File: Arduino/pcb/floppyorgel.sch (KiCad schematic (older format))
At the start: 2 parts, among them J1 VCC_Power_Select

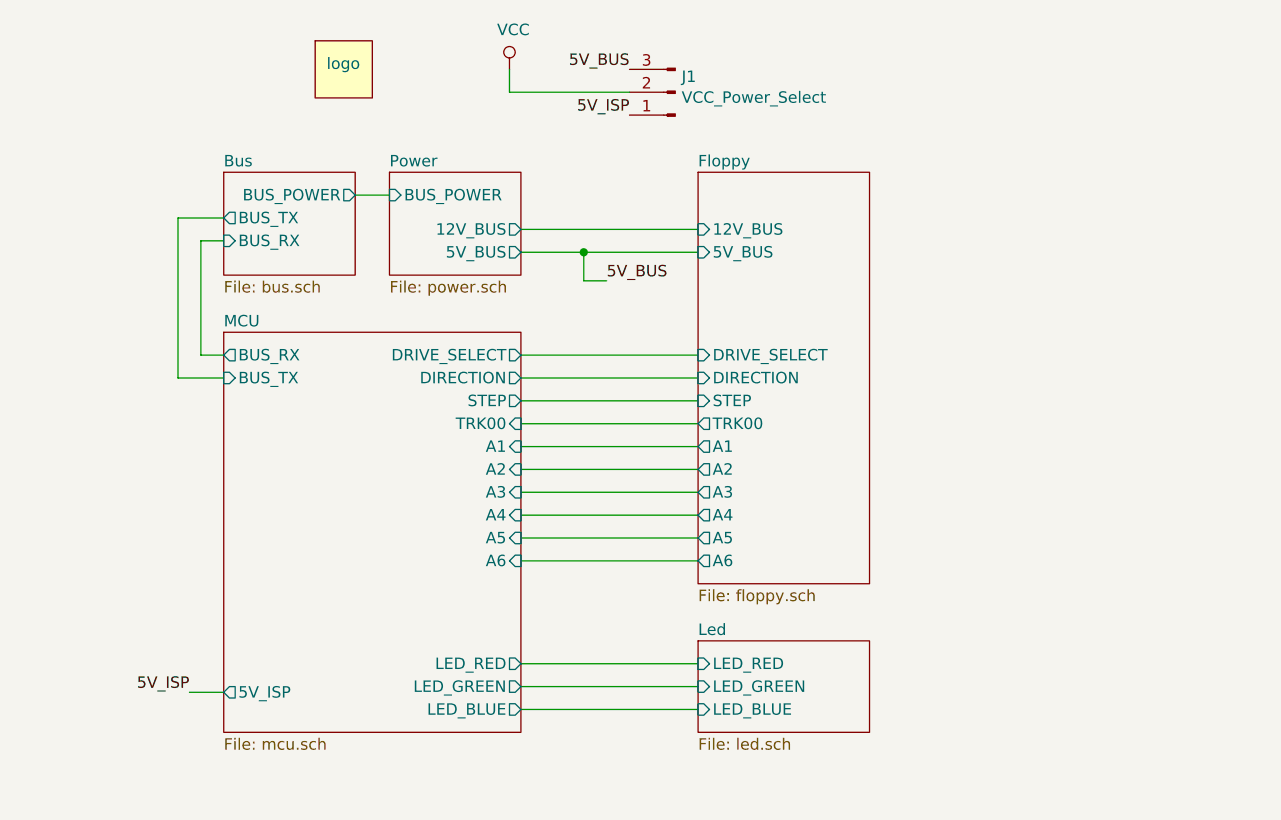
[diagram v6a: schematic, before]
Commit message: pcb: route RS485 control pins
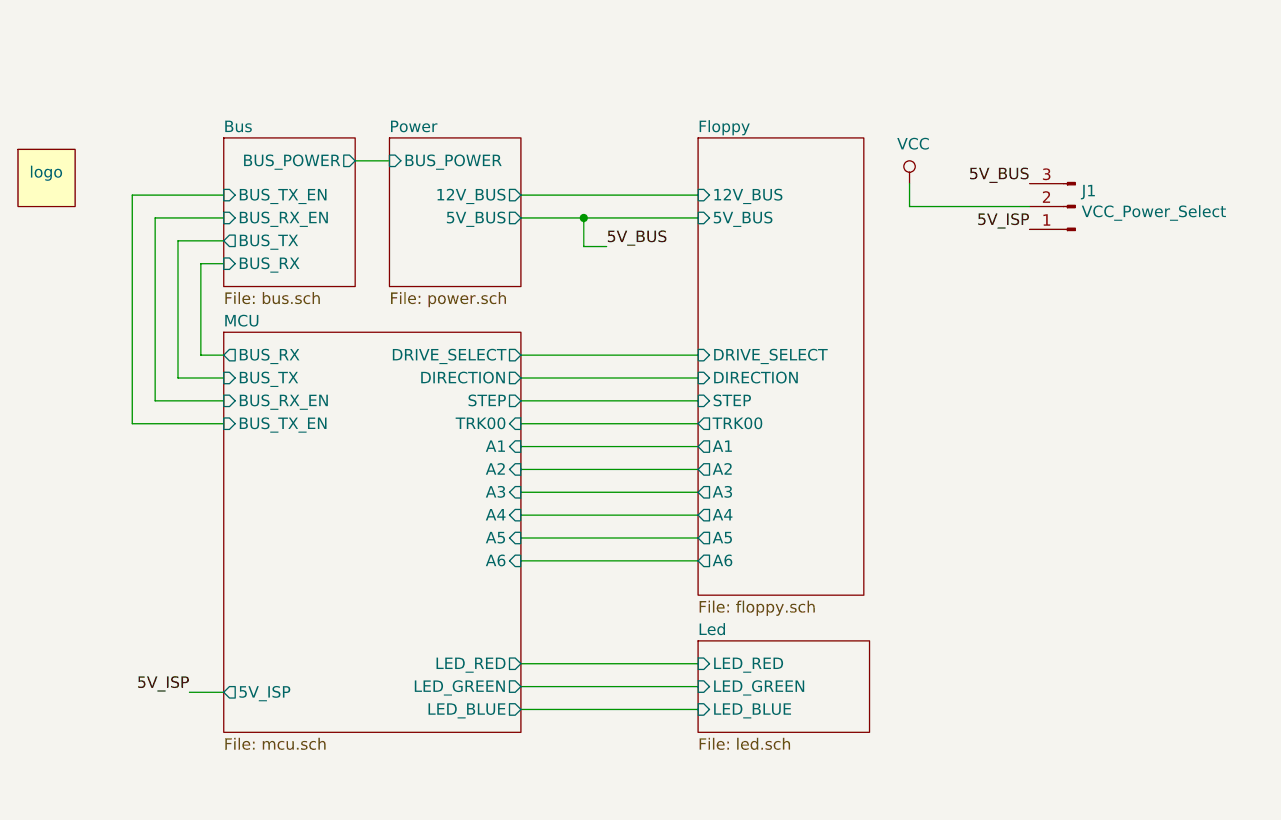
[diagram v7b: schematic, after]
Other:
- moved on the sheet: J1
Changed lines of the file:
@@
 $EndDescr
 $Sheet
-S 3725 2775 575  450
-U 5CD1E0A5
-F0 "Bus" 50
-F1 "bus.sch" 50
-F2 "BUS_POWER" O R 4300 2875 50
-F3 "BUS_TX" O L 3725 2975 50
-F4 "BUS_RX" I L 3725 3075 50
-$EndSheet
-$Sheet
-S 4450 2775 575  450
+S 4450 2625 575  650
 U 5CD31258
 F0 "Power" 50
 F1 "power.sch" 50
-F2 "BUS_POWER" I L 4450 2875 50
-F3 "12V_BUS" O R 5025 3025 50
-F4 "5V_BUS" O R 5025 3125 50
+F2 "BUS_POWER" I L 4450 2725 50
+F3 "12V_BUS" O R 5025 2875 50
+F4 "5V_BUS" O R 5025 2975 50
 $EndSheet
 Wire Wire Line
@@
 	3725 3675 3525 3675
 Wire Wire Line
-	4300 2875 4450 2875
-Wire Wire Line
-	3725 3075 3625 3075
-Wire Wire Line
-	3625 3075 3625 3575
-Wire Wire Line
-	3525 2975 3725 2975
-Wire Wire Line
-	3525 2975 3525 3675
-Wire Wire Line
-	5025 3025 5800 3025
-Wire Wire Line
 	5025 3575 5800 3575
 Wire Wire Line
 	5025 3675 5800 3675
-Wire Wire Line
-	5025 3125 5300 3125
-Text Label 5400 3250 0    50   ~ 0
+Text Label 5400 3100 0    50   ~ 0
 5V_BUS
-Wire Wire Line
-	5400 3250 5300 3250
-Wire Wire Line
-	5300 3250 5300 3125
-Connection ~ 5300 3125
-Wire Wire Line
-	5300 3125 5800 3125
 $Sheet
 S 5800 4825 750  400
@@
 L logo:logo L1
 U 1 1 5CDF6702
-P 4250 2325
-F 0 "L1" H 4250 2400 50  0001 C CNN
-F 1 "logo" H 4175 2350 50  0000 L CNN
-F 2 "logo:logo" H 4250 2325 50  0001 C CNN
-F 3 "" H 4250 2325 50  0001 C CNN
-	1    4250 2325
+P 2950 2800
+F 0 "L1" H 2950 2875 50  0001 C CNN
+F 1 "logo" H 2875 2825 50  0000 L CNN
+F 2 "logo:logo" H 2950 2800 50  0001 C CNN
+F 3 "" H 2950 2800 50  0001 C CNN
+	1    2950 2800
 	1    0    0    -1
 $EndComp
-Text Label 5500 2325 2    50   ~ 0
+Text Label 7250 2825 2    50   ~ 0
 5V_BUS
-Text Label 5500 2525 2    50   ~ 0
+Text Label 7250 3025 2    50   ~ 0
 5V_ISP
 $Comp
 L vcc_power_select:VCC_Power_Select J1
 U 1 1 5D19C0BF
-P 5700 2425
-F 0 "J1" H 5672 2357 50  0000 R CNN
-F 1 "VCC_Power_Select" H 5672 2448 50  0000 R CNN
-F 2 "w_switch:switch_mmp122-r" H 5700 2425 50  0001 C CNN
-F 3 "~" H 5700 2425 50  0001 C CNN
-	1    5700 2425
+P 7450 2925
+F 0 "J1" H 7422 2857 50  0000 R CNN
+F 1 "VCC_Power_Select" H 7422 2948 50  0000 R CNN
+F 2 "w_switch:switch_mmp122-r" H 7450 2925 50  0001 C CNN
+F 3 "~" H 7450 2925 50  0001 C CNN
+	1    7450 2925
 	-1   0    0    1
 $EndComp
 Wire Wire Line
-	4975 2425 5500 2425
+	6725 2925 7250 2925
 Wire Wire Line
-	4975 2325 4975 2425
+	6725 2825 6725 2925
 $Comp
 L power:VCC #PWR01
 U 1 1 5D10B089
-P 4975 2325
+P 6725 2825
 AR Path="/5D10B089" Ref="#PWR01"  Part="1"
 AR Path="/5CD31258/5D10B089" Ref="#PWR?"  Part="1"
-F 0 "#PWR01" H 4975 2175 50  0001 C CNN
-F 1 "VCC" H 4992 2498 50  0000 C CNN
-F 2 "" H 4975 2325 50  0001 C CNN
-F 3 "" H 4975 2325 50  0001 C CNN
-	1    4975 2325
+F 0 "#PWR01" H 6725 2675 50  0001 C CNN
+F 1 "VCC" H 6742 2998 50  0000 C CNN
+F 2 "" H 6725 2825 50  0001 C CNN
+F 3 "" H 6725 2825 50  0001 C CNN
+	1    6725 2825
 	1    0    0    -1
 $EndComp
-$Sheet
-S 5800 2775 750  1800
-U 5CD0EE48
-F0 "Floppy" 50
-F1 "floppy.sch" 50
-F2 "DRIVE_SELECT" I L 5800 3575 50
-F3 "DIRECTION" I L 5800 3675 50
-F4 "TRK00" O L 5800 3875 50
-F5 "STEP" I L 5800 3775 50
-F6 "5V_BUS" I L 5800 3125 50
-F7 "12V_BUS" I L 5800 3025 50
-F8 "A4" O L 5800 4275 50
-F9 "A5" O L 5800 4375 50
-F10 "A6" O L 5800 4475 50
-F11 "A3" O L 5800 4175 50
-F12 "A2" O L 5800 4075 50
-F13 "A1" O L 5800 3975 50
-$EndSheet
 Wire Wire Line
 	5025 4925 5800 4925
@@
 F16 "LED_GREEN" O R 5025 5025 50
 F17 "LED_BLUE" O R 5025 5125 50
+F18 "BUS_TX_EN" I L 3725 3875 50
+F19 "BUS_RX_EN" I L 3725 3775 50
 $EndSheet
+$Sheet
+S 3725 2625 575  650
+U 5CD1E0A5
+F0 "Bus" 50
+F1 "bus.sch" 50
+F2 "BUS_POWER" O R 4300 2725 50
+F3 "BUS_TX" O L 3725 3075 50
+F4 "BUS_RX" I L 3725 3175 50
+F5 "BUS_RX_EN" I L 3725 2975 50
+F6 "BUS_TX_EN" I L 3725 2875 50
+$EndSheet
+Wire Wire Line
+	3625 3575 3625 3175
+Wire Wire Line
+	3625 3175 3725 3175
+Wire Wire Line
+	3725 3075 3525 3075
+Wire Wire Line
+	3525 3075 3525 3675
+Wire Wire Line
+	3725 3775 3425 3775
+Wire Wire Line
+	3425 3775 3425 2975
+Wire Wire Line
+	3425 2975 3725 2975
+Wire Wire Line
+	3725 3875 3325 3875
+Wire Wire Line
+	3325 3875 3325 2875
+Wire Wire Line
+	3325 2875 3725 2875
+Wire Wire Line
+	4300 2725 4450 2725
+$Sheet
+S 5800 2625 725  2000
+U 5CD0EE48
+F0 "Floppy" 50
+F1 "floppy.sch" 50
+F2 "DRIVE_SELECT" I L 5800 3575 50
+F3 "DIRECTION" I L 5800 3675 50
+F4 "TRK00" O L 5800 3875 50
+F5 "STEP" I L 5800 3775 50
+F6 "5V_BUS" I L 5800 2975 50
+F7 "12V_BUS" I L 5800 2875 50
+F8 "A4" O L 5800 4275 50
+F9 "A5" O L 5800 4375 50
+F10 "A6" O L 5800 4475 50
+F11 "A3" O L 5800 4175 50
+F12 "A2" O L 5800 4075 50
+F13 "A1" O L 5800 3975 50
+$EndSheet
+Wire Wire Line
+	5025 2875 5800 2875
+Wire Wire Line
+	5025 2975 5300 2975
+Wire Wire Line
+	5300 2975 5300 3100
+Wire Wire Line
+	5300 3100 5400 3100
+Connection ~ 5300 2975
+Wire Wire Line
+	5300 2975 5800 2975
 $EndSCHEMATC
